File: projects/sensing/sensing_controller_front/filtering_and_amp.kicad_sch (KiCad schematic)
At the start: 17 parts, among them U4 AD8630

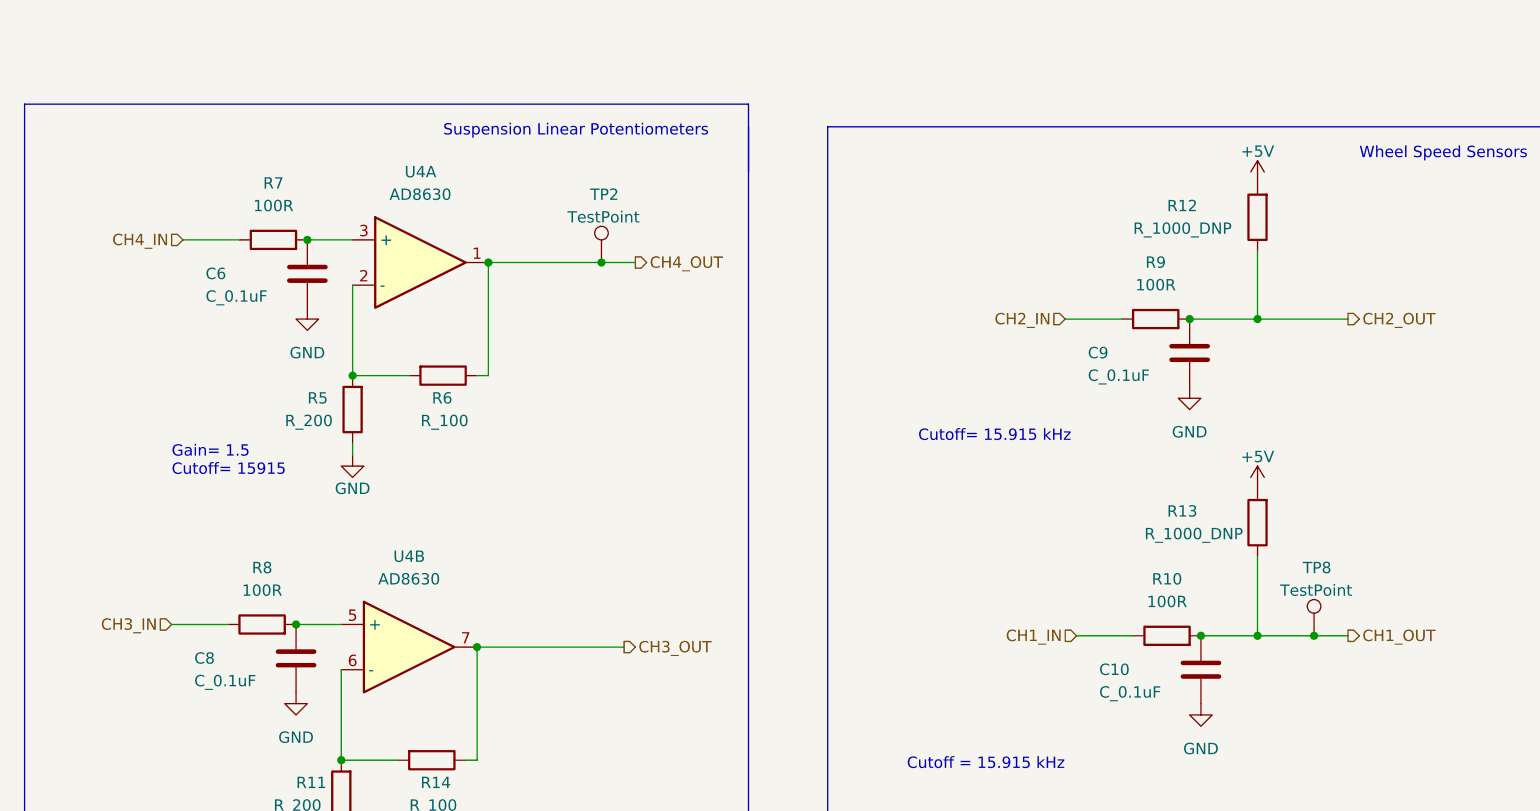
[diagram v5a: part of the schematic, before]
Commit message: completed all rev2 feedback changes
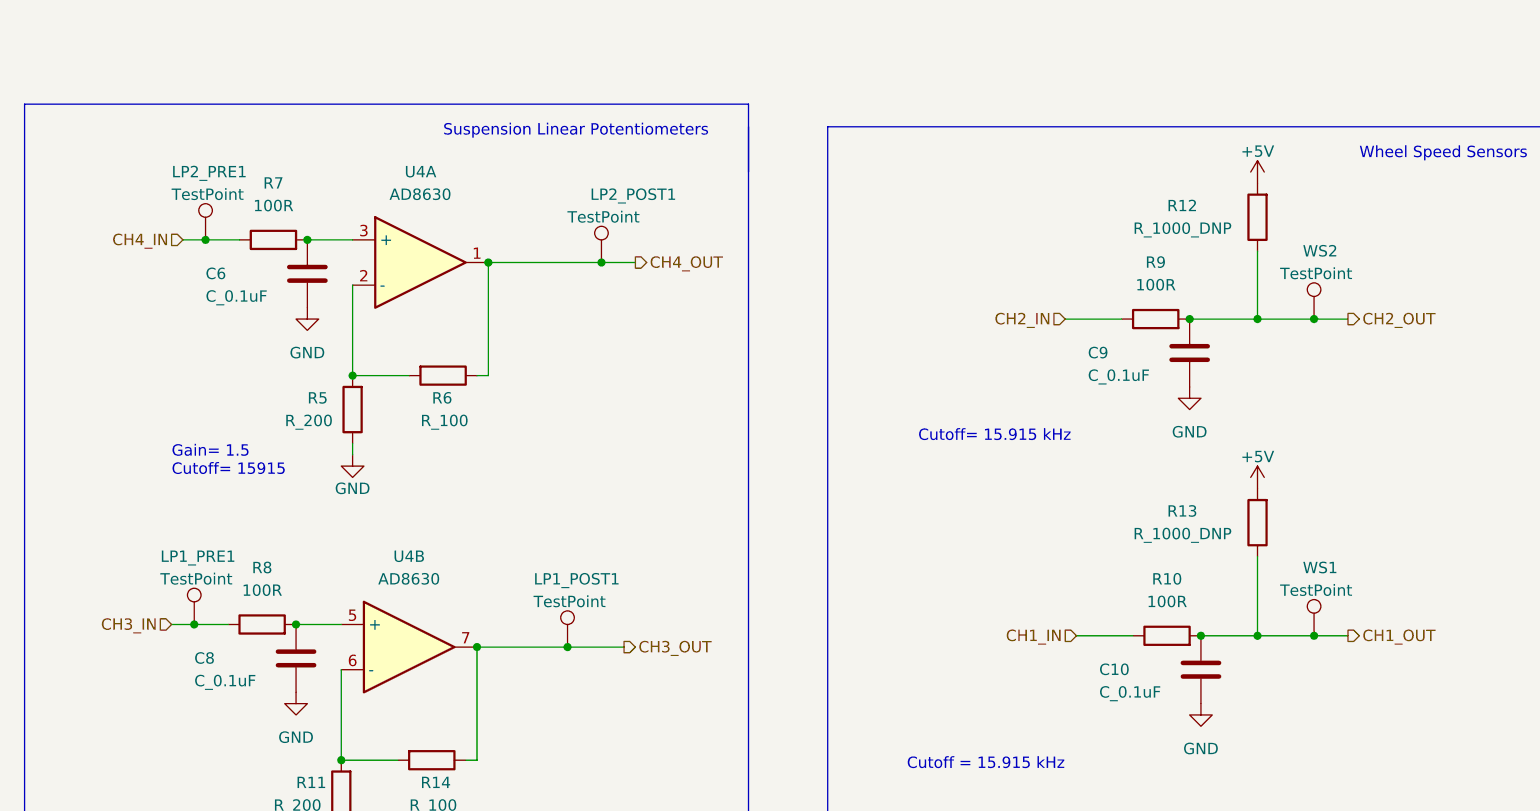
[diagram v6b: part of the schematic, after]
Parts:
- added LP1_POST1, LP1_PRE1, LP2_PRE1, WS2: TestPoint, TestPoint:TestPoint_Pad_D1.0mm, symbol Connector:TestPoint
- renumbered TP2 to LP2_POST1, TP8 to WS1
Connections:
- net CH2_OUT: now also WS2.1
- net CH3_IN: now also LP1_PRE1.1
- net CH3_OUT: now also LP1_POST1.1
- net CH4_IN: now also LP2_PRE1.1
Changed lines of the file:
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@@
   (junction (at 167.64 85.09) (diameter 0) (color 0 0 0 0)
   )
+  (junction (at 163.83 128.27) (diameter 0) (color 0 0 0 0)
+  )
   (junction (at 134.62 82.55) (diameter 0) (color 0 0 0 0)
   )
   (junction (at 241.3 91.44) (diameter 0) (color 0 0 0 0)
   )
+  (junction (at 121.92 125.73) (diameter 0) (color 0 0 0 0)
+  )
   (junction (at 233.68 91.44) (diameter 0) (color 0 0 0 0)
   )
   (junction (at 241.3 127) (diameter 0) (color 0 0 0 0)
   )
+  (junction (at 123.19 82.55) (diameter 0) (color 0 0 0 0)
+  )
   (junction (at 139.7 97.79) (diameter 0) (color 0 0 0 0)
   )
@@
   )
   (junction (at 138.43 140.97) (diameter 0) (color 0 0 0 0)
+  )
+  (junction (at 247.65 91.44) (diameter 0) (color 0 0 0 0)
   )
   (junction (at 234.95 127) (diameter 0) (color 0 0 0 0)
@@
     (stroke (width 0) (type default) (color 0 0 0 0))
   )
-  (wire (pts (xy 241.3 91.44) (xy 251.46 91.44))
+  (wire (pts (xy 241.3 91.44) (xy 247.65 91.44))
     (stroke (width 0) (type default) (color 0 0 0 0))
   )
@@
     (stroke (width 0) (type default) (color 0 0 0 0))
   )
+  (wire (pts (xy 123.19 82.55) (xy 127 82.55))
+    (stroke (width 0) (type default) (color 0 0 0 0))
+  )
   (polyline (pts (xy 275.59 154.94) (xy 275.59 69.85))
     (stroke (width 0) (type default) (color 0 0 0 0))
@@
     (stroke (width 0) (type default) (color 0 0 0 0))
   )
-  (wire (pts (xy 120.65 82.55) (xy 127 82.55))
+  (wire (pts (xy 120.65 82.55) (xy 123.19 82.55))
     (stroke (width 0) (type default) (color 0 0 0 0))
   )
@@
     (stroke (width 0) (type default) (color 0 0 0 0))
   )
-  (wire (pts (xy 153.67 128.27) (xy 170.18 128.27))
+  (wire (pts (xy 153.67 128.27) (xy 163.83 128.27))
     (stroke (width 0) (type default) (color 0 0 0 0))
   )
@@
     (stroke (width 0) (type default) (color 0 0 0 0))
   )
+  (wire (pts (xy 247.65 91.44) (xy 251.46 91.44))
+    (stroke (width 0) (type default) (color 0 0 0 0))
+  )
   (wire (pts (xy 138.43 149.86) (xy 138.43 148.59))
     (stroke (width 0) (type default) (color 0 0 0 0))
@@
     (stroke (width 0) (type default) (color 0 0 0 0))
   )
-  (wire (pts (xy 119.38 125.73) (xy 125.73 125.73))
+  (wire (pts (xy 119.38 125.73) (xy 121.92 125.73))
     (stroke (width 0) (type default) (color 0 0 0 0))
   )
@@
     (stroke (width 0) (type default) (color 0 0 0 0))
   )
+  (wire (pts (xy 121.92 125.73) (xy 125.73 125.73))
+    (stroke (width 0) (type default) (color 0 0 0 0))
+  )
   (polyline (pts (xy 86.36 72.39) (xy 54.61 72.39))
     (stroke (width 0) (type default) (color 0 0 0 0))
@@
   )
   (wire (pts (xy 233.68 91.44) (xy 241.3 91.44))
+    (stroke (width 0) (type default) (color 0 0 0 0))
+  )
+  (wire (pts (xy 163.83 128.27) (xy 170.18 128.27))
     (stroke (width 0) (type default) (color 0 0 0 0))
   )
@@
     (pin "1")
     (pin "2")
+  )
+  (symbol (lib_id "Connector:TestPoint") (at 247.65 91.44 0) (unit 1)
+    (in_bom yes) (on_board yes)
+    (property "Reference" "WS2" (id 0) (at 246.38 83.82 0)
+      (effects (font (size 1.27 1.27)) (justify left))
+    )
+    (property "Value" "TestPoint" (id 1) (at 243.84 86.36 0)
+      (effects (font (size 1.27 1.27)) (justify left))
+    )
+    (property "Footprint" "TestPoint:TestPoint_Pad_D1.0mm" (id 2) (at 252.73 91.44 0)
+      (effects (font (size 1.27 1.27)) hide)
+    )
+    (property "Datasheet" "~" (id 3) (at 252.73 91.44 0)
+      (effects (font (size 1.27 1.27)) hide)
+    )
+    (pin "1")
   )
   (symbol (lib_id "formula:AD8630") (at 147.32 85.09 0) (unit 1)
@@
     (pin "2")
   )
+  (symbol (lib_id "Connector:TestPoint") (at 163.83 128.27 0) (unit 1)
+    (in_bom yes) (on_board yes)
+    (property "Reference" "LP1_POST1" (id 0) (at 160.02 120.65 0)
+      (effects (font (size 1.27 1.27)) (justify left))
+    )
+    (property "Value" "TestPoint" (id 1) (at 160.02 123.19 0)
+      (effects (font (size 1.27 1.27)) (justify left))
+    )
+    (property "Footprint" "TestPoint:TestPoint_Pad_D1.0mm" (id 2) (at 168.91 128.27 0)
+      (effects (font (size 1.27 1.27)) hide)
+    )
+    (property "Datasheet" "~" (id 3) (at 168.91 128.27 0)
+      (effects (font (size 1.27 1.27)) hide)
+    )
+    (pin "1")
+  )
   (symbol (lib_id "power:GND") (at 139.7 106.68 0) (unit 1)
     (in_bom yes) (on_board yes)
@@
   (symbol (lib_id "Connector:TestPoint") (at 167.64 85.09 0) (unit 1)
     (in_bom yes) (on_board yes)
-    (property "Reference" "TP2" (id 0) (at 166.37 77.47 0)
+    (property "Reference" "LP2_POST1" (id 0) (at 166.37 77.47 0)
       (effects (font (size 1.27 1.27)) (justify left))
     )
@@
     (pin "1")
   )
+  (symbol (lib_id "Connector:TestPoint") (at 123.19 82.55 0) (unit 1)
+    (in_bom yes) (on_board yes)
+    (property "Reference" "LP2_PRE1" (id 0) (at 119.38 74.93 0)
+      (effects (font (size 1.27 1.27)) (justify left))
+    )
+    (property "Value" "TestPoint" (id 1) (at 119.38 77.47 0)
+      (effects (font (size 1.27 1.27)) (justify left))
+    )
+    (property "Footprint" "TestPoint:TestPoint_Pad_D1.0mm" (id 2) (at 128.27 82.55 0)
+      (effects (font (size 1.27 1.27)) hide)
+    )
+    (property "Datasheet" "~" (id 3) (at 128.27 82.55 0)
+      (effects (font (size 1.27 1.27)) hide)
+    )
+    (pin "1")
+  )
   (symbol (lib_id "OEM:100R") (at 231.14 127 90) (unit 1)
     (in_bom yes) (on_board yes)
@@
     (pin "1")
   )
+  (symbol (lib_id "Connector:TestPoint") (at 121.92 125.73 0) (unit 1)
+    (in_bom yes) (on_board yes)
+    (property "Reference" "LP1_PRE1" (id 0) (at 118.11 118.11 0)
+      (effects (font (size 1.27 1.27)) (justify left))
+    )
+    (property "Value" "TestPoint" (id 1) (at 118.11 120.65 0)
+      (effects (font (size 1.27 1.27)) (justify left))
+    )
+    (property "Footprint" "TestPoint:TestPoint_Pad_D1.0mm" (id 2) (at 127 125.73 0)
+      (effects (font (size 1.27 1.27)) hide)
+    )
+    (property "Datasheet" "~" (id 3) (at 127 125.73 0)
+      (effects (font (size 1.27 1.27)) hide)
+    )
+    (pin "1")
+  )
   (symbol (lib_id "formula:R_200") (at 139.7 101.6 180) (unit 1)
     (in_bom yes) (on_board yes)
@@
       (effects (font (size 1.27 1.27)) (justify right))
     )
-    (property "Value" "R_1000_DNP" (id 1) (at 228.6 115.57 0)
+    (property "Value" "R_1000_DNP" (id 1) (at 227.33 115.57 0)
       (effects (font (size 1.27 1.27)) (justify right))
     )
@@
   (symbol (lib_id "Connector:TestPoint") (at 247.65 127 0) (unit 1)
     (in_bom yes) (on_board yes)
-    (property "Reference" "TP8" (id 0) (at 246.38 119.38 0)
-      (effects (font (size 1.27 1.27)) (justify left))
-    )
+    (property "Reference" "WS1" (id 0) (at 246.38 119.38 0)
+      (effects (font (size 1.27 1.27)) (justify left))
+    )
